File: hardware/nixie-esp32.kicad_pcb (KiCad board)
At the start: 6 copper layers, 70.5 x 70 mm, 53 parts, among them J1 USB4216-03-A_REVA, SW1 RESET, SW2 BOOT, U1 AP7361C-33E-13, U2 ESP32-S3-WROOM-1, U3 SN74AHCT1G125DBVR, U4 SN74141N, U5 SN74141N, U6 SN74141N

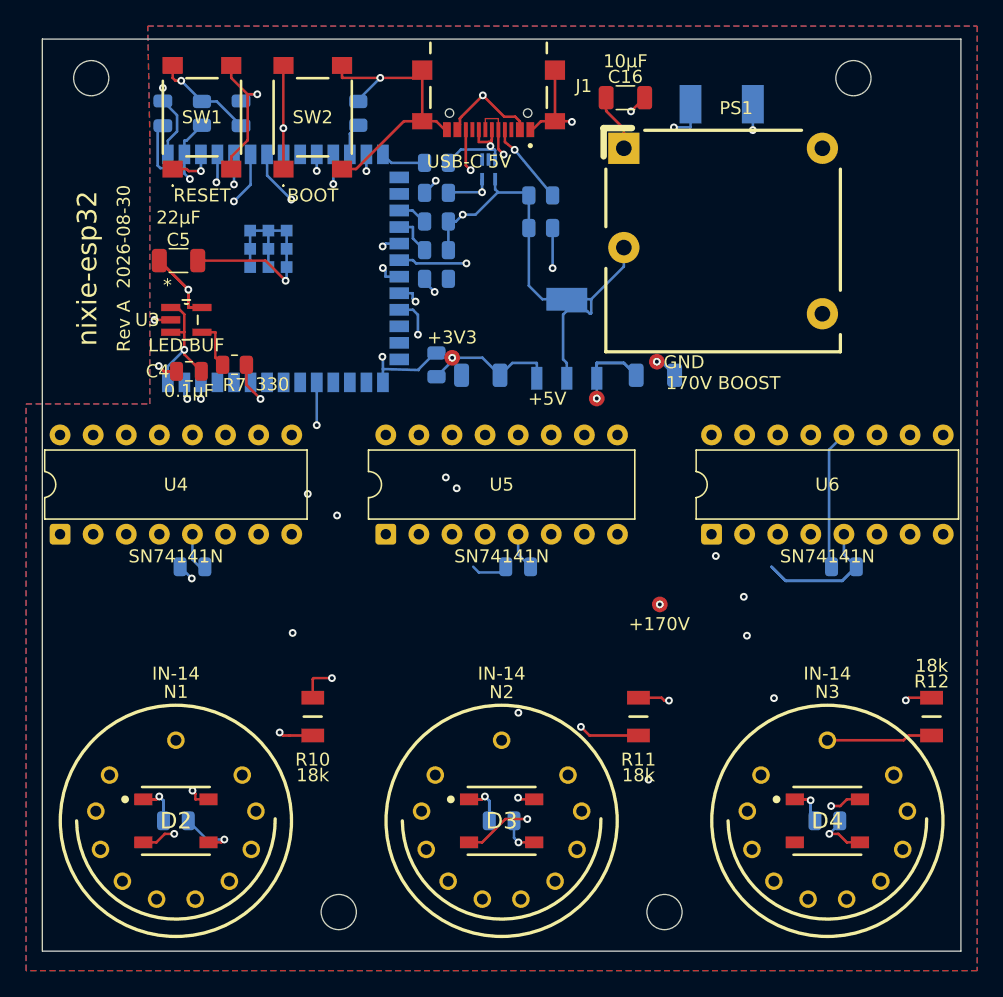
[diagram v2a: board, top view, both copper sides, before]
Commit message: Add 5V and 170V status LED indicators
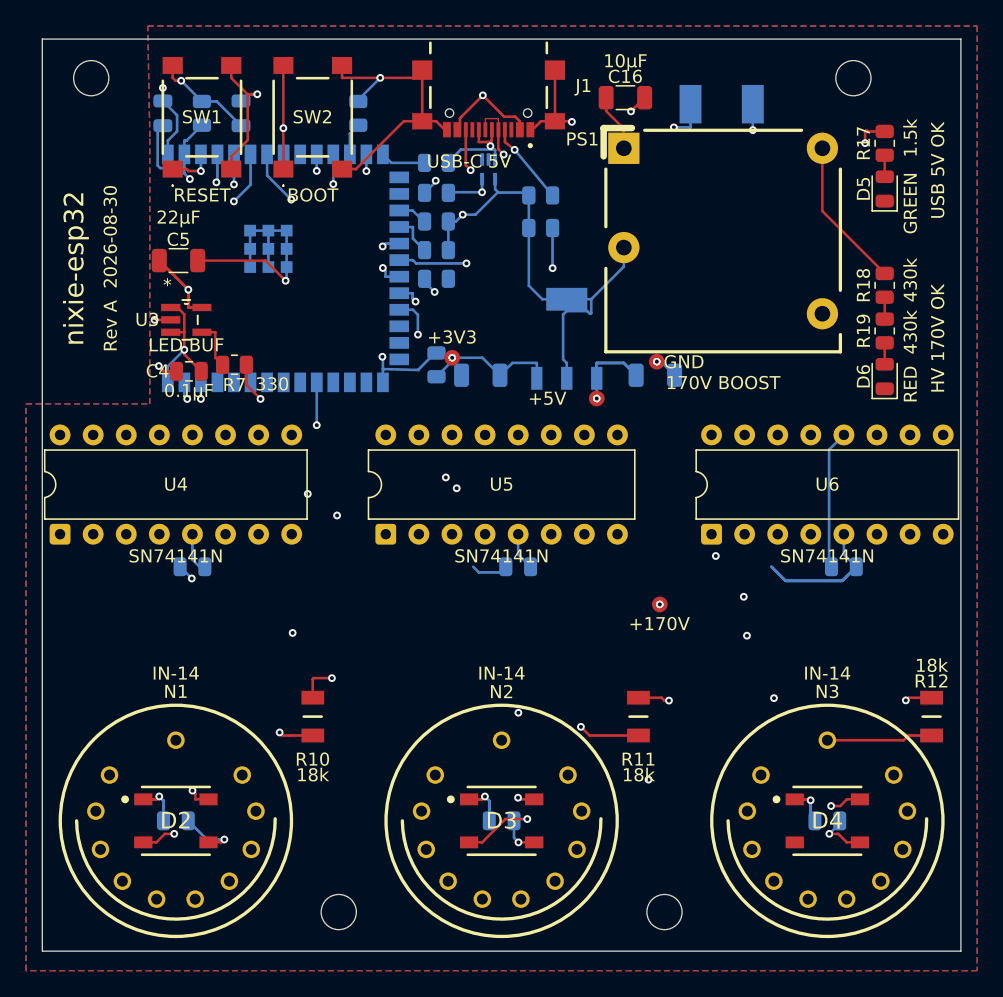
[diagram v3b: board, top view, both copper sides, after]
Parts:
- added D5: GREEN, LED_SMD:LED_0805_2012Metric, F.Cu at (183.4, 88.0)
- added D6: RED, LED_SMD:LED_0805_2012Metric, F.Cu at (183.4, 102.4)
- added R17: 1.5k, Resistor_SMD:R_0805_2012Metric, F.Cu at (183.4, 84.5)
- added R18: 430k, Resistor_SMD:R_0805_2012Metric, F.Cu at (183.4, 95.4)
- added R19: 430k, Resistor_SMD:R_0805_2012Metric, F.Cu at (183.4, 98.9)
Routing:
- net +170V: track 101.2 -> 112.8 mm
- net +5V: track 248.2 -> 250.7 mm, vias 7 -> 8
- net /Nixies/Power170v/HV_LED_DIV: track 0.00 -> 1.67 mm
- net Net-(D6-A): track 0.00 -> 1.65 mm
- net Net-(D5-A): track 0.00 -> 1.65 mm
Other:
- board text added: "HV 170V OK"
- board text added: "USB 5V OK"
